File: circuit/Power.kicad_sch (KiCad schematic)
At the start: 40 parts, among them J2 XT30, SW2 EG1271, U3 HSBA3119, U4 TPSM84209RKHT, U5 LM2733YMF, U6 TPS7A9201DSKR

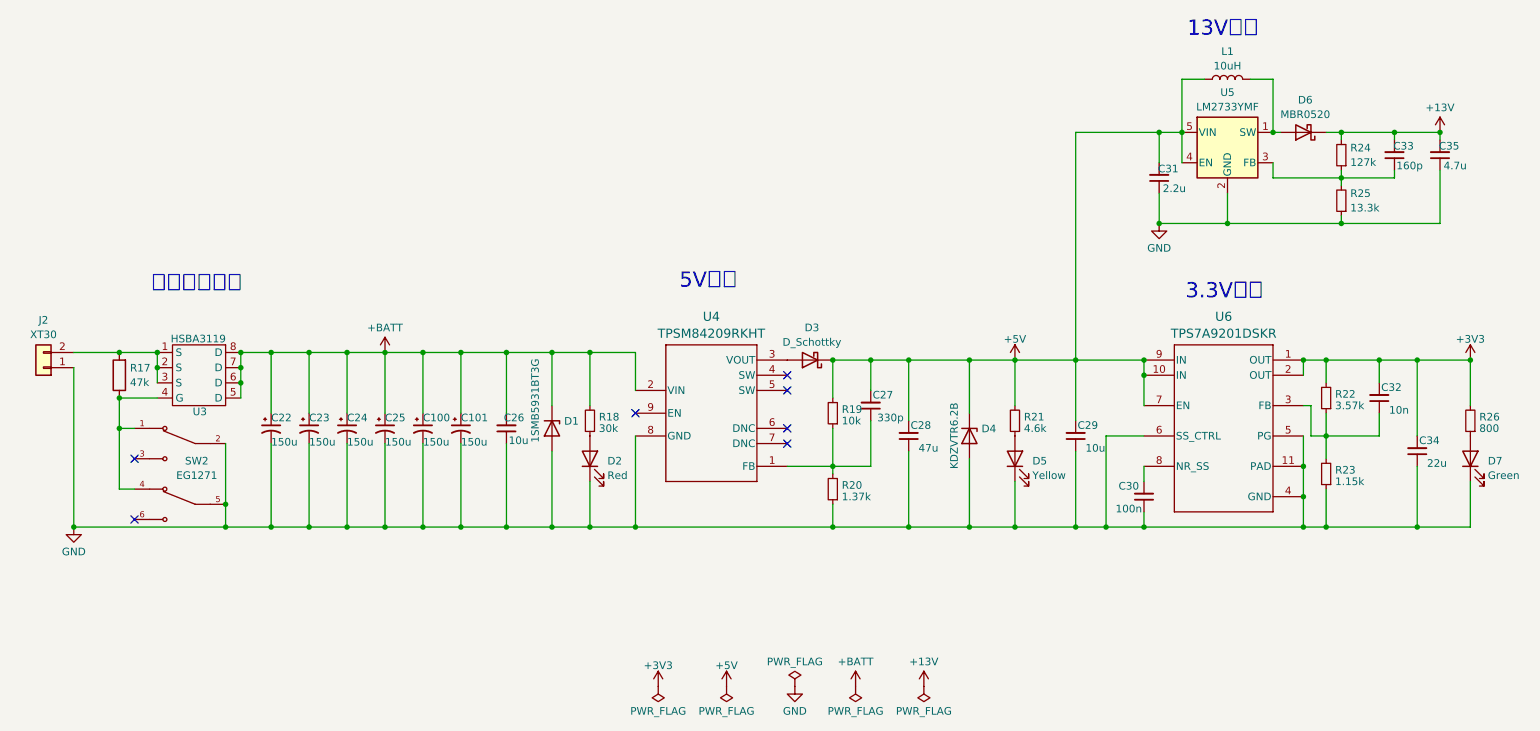
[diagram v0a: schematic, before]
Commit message: スマコンの設定変更 回路図変更
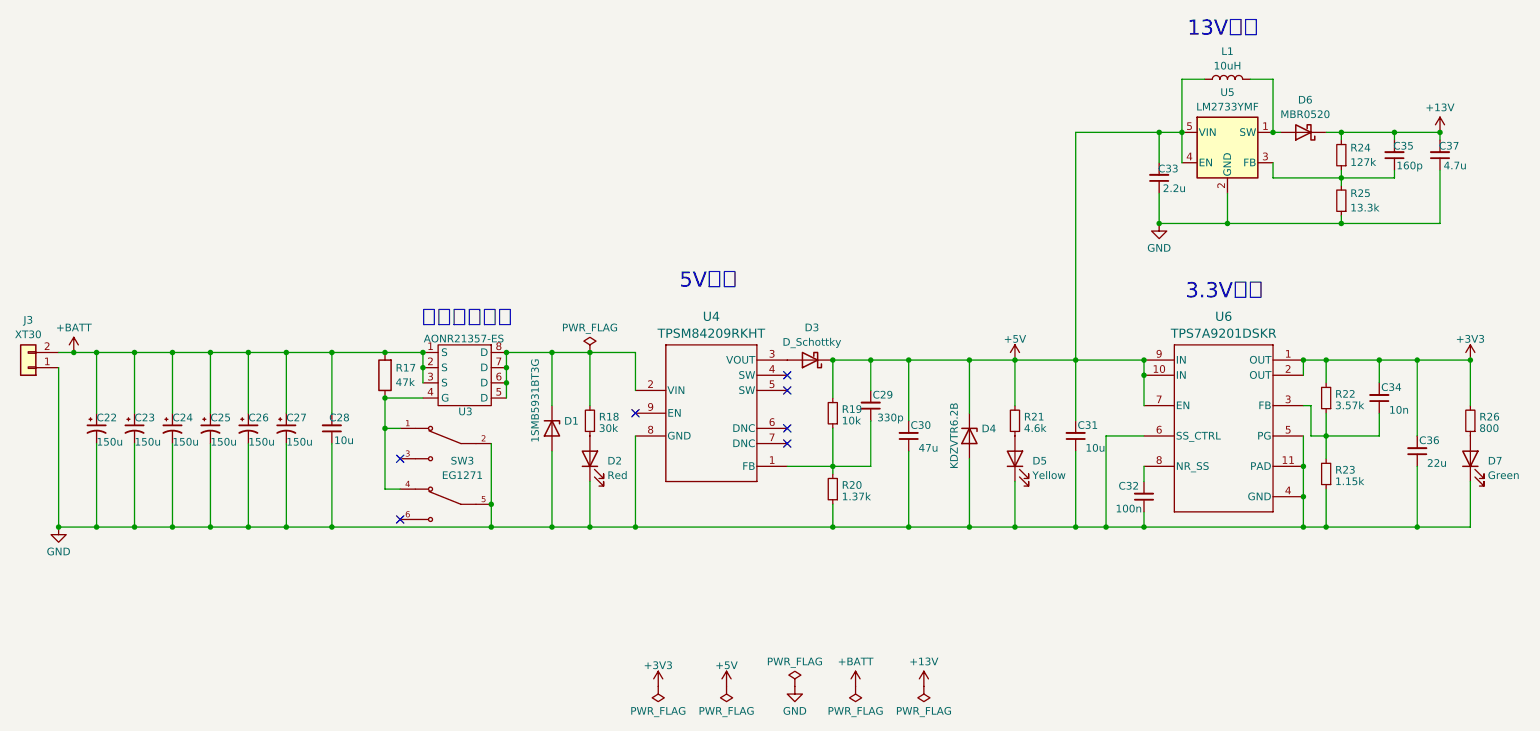
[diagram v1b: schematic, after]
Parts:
- SW3: renamed from SW2; symbol robocon:EG1271 -> robot_contest:EG1271
- U3: value HSBA3119 -> AONR21357-ES; footprint robot_contest:IRFH7084TRPBF_INF -> robot_contest:AONR21357-ES; symbol robocon:ESN7403 -> robot_contest:ESN7403
- U4: symbol robocon:TPSM84209RKHT -> robot_contest:TPSM84209RKHT
- U6: symbol robocon:TPS7A9201DSKT -> robot_contest:TPS7A9201DSKT
- renumbered C100 to C26, C101 to C27, C26 to C28, C27 to C29, C28 to C30, C29 to C31, C30 to C32, C31 to C33, C32 to C34, C33 to C35, C34 to C36, C35 to C37, J2 to J3
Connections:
- net +BATT: now also J3.2 (Pin_2), R17.2, U3.1 (S), U3.2 (S), U3.3 (S); no longer D1.1 (K), R18.2, U3.5 (D), U3.6 (D), U3.7 (D), U3.8 (D), U4.2 (VIN)
- new net: D1.1 (K), R18.2, U3.5 (D), U3.6 (D), U3.7 (D), U3.8 (D), U4.2 (VIN)
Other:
- moved on the sheet: C22, C23, C24, C25, C26, C27, C28, J3, R17, SW3, U3
